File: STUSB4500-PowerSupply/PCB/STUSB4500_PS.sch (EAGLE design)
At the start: 90 parts, among them J2 FEMALE 2x3, J3 FEMALE 2x3, J4 FEMALE 2x3

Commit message: UART and 3V3
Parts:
- added F1: 6V/0.5A, DD_SparkFun-Fuses:PPTC_HALF-AMP
- added J9: (no value), DD_SparkFun-Connectors:CONN_03LOCK_NO_SILK
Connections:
- new net UART_RX: J9.2, U$8.PA1/ADC_IN1/COMP1_INP/USART4_RX
- new net UART_TX: J9.1, U$8.PA2/ADC_IN2/WKUP4USART2_TX
- net +3V3: now also F1.2
- net GND: now also J9.3
- net VIN_2: now also F1.1
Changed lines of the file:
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@@
 <setting verticaltext="up"/>
 </settings>
-<grid distance="0.1" unitdist="inch" unit="inch" style="lines" multiple="1" display="no" altdistance="0.01" altunitdist="inch" altunit="inch"/>
+<grid distance="0.05" unitdist="inch" unit="inch" style="lines" multiple="1" display="no" altdistance="0.01" altunitdist="inch" altunit="inch"/>
 <layers>
 <layer number="1" name="Top" color="4" fill="1" visible="no" active="no"/>
@@
 <part name="+3V15" library="supply1" library_urn="urn:adsk.eagle:library:371" deviceset="+3V3" device=""/>
 <part name="GND5" library="supply1" library_urn="urn:adsk.eagle:library:371" deviceset="GND" device=""/>
+<part name="J9" library="DD_SparkFun-Connectors" deviceset="CONN_03" device="LOCK_NO_SILK"/>
+<part name="GND6" library="supply1" library_urn="urn:adsk.eagle:library:371" deviceset="GND" device=""/>
+<part name="F1" library="DD_SparkFun-Fuses" deviceset="PPTC" device="_HALF-AMP" value="6V/0.5A"/>
+<part name="+3V16" library="supply1" library_urn="urn:adsk.eagle:library:371" deviceset="+3V3" device=""/>
 </parts>
 <sheets>
@@
 <attribute name="VALUE" x="231.14" y="48.26" size="1.778" layer="96"/>
 </instance>
+<instance part="J9" gate="J$1" x="219.71" y="147.32" smashed="yes" rot="R180">
+<attribute name="VALUE" x="222.25" y="154.686" size="1.778" layer="96" font="vector" rot="R180"/>
+<attribute name="NAME" x="222.25" y="141.732" size="1.778" layer="95" font="vector" rot="R180"/>
+</instance>
+<instance part="GND6" gate="1" x="209.55" y="139.7" smashed="yes">
+<attribute name="VALUE" x="207.01" y="137.16" size="1.778" layer="96"/>
+</instance>
+<instance part="F1" gate="G$1" x="53.34" y="152.4" smashed="yes">
+<attribute name="NAME" x="55.245" y="155.575" size="1.778" layer="95" font="vector" align="bottom-center"/>
+<attribute name="VALUE" x="54.61" y="149.606" size="1.778" layer="96" font="vector" align="top-center"/>
+</instance>
+<instance part="+3V16" gate="G$1" x="62.23" y="156.21" smashed="yes">
+<attribute name="VALUE" x="59.69" y="156.21" size="1.778" layer="96"/>
+</instance>
 </instances>
 <busses>
@@
 <wire x1="213.36" y1="104.14" x2="213.36" y2="96.52" width="0.1524" layer="91"/>
 <junction x="213.36" y="96.52"/>
+<junction x="226.06" y="96.52"/>
 </segment>
 </net>
@@
 <wire x1="210.82" y1="99.06" x2="226.06" y2="99.06" width="0.1524" layer="91"/>
 <label x="218.44" y="99.06" size="1.778" layer="95"/>
+<junction x="226.06" y="99.06"/>
 </segment>
 </net>
@@
 <pinref part="GND5" gate="1" pin="GND"/>
 </segment>
+<segment>
+<pinref part="J9" gate="J$1" pin="3"/>
+<wire x1="212.09" y1="144.78" x2="209.55" y2="144.78" width="0.1524" layer="91"/>
+<pinref part="GND6" gate="1" pin="GND"/>
+<wire x1="209.55" y1="144.78" x2="209.55" y2="142.24" width="0.1524" layer="91"/>
+</segment>
 </net>
 <net name="+3V3" class="0">
@@
 <wire x1="68.58" y1="83.82" x2="68.58" y2="86.36" width="0.1524" layer="91"/>
 </segment>
+<segment>
+<pinref part="F1" gate="G$1" pin="2"/>
+<wire x1="60.96" y1="152.4" x2="62.23" y2="152.4" width="0.1524" layer="91"/>
+<pinref part="+3V16" gate="G$1" pin="+3V3"/>
+<wire x1="62.23" y1="152.4" x2="62.23" y2="153.67" width="0.1524" layer="91"/>
+</segment>
 </net>
 <net name="SWDIO" class="0">
@@
 <wire x1="38.1" y1="119.38" x2="45.72" y2="119.38" width="0.1524" layer="91"/>
 <label x="40.64" y="119.38" size="1.778" layer="95"/>
+<junction x="45.72" y="119.38"/>
 </segment>
 </net>
@@
 <wire x1="38.1" y1="116.84" x2="45.72" y2="116.84" width="0.1524" layer="91"/>
 <label x="40.64" y="116.84" size="1.778" layer="95"/>
+<junction x="45.72" y="116.84"/>
 </segment>
 </net>
@@
 <wire x1="38.1" y1="114.3" x2="45.72" y2="114.3" width="0.1524" layer="91"/>
 <label x="40.64" y="114.3" size="1.778" layer="95"/>
+<junction x="45.72" y="114.3"/>
 </segment>
 </net>
@@
 <pinref part="R31" gate="G$1" pin="1"/>
 <pinref part="D2" gate="G$1" pin="A"/>
+<junction x="236.22" y="106.68"/>
 </segment>
 </net>
@@
 <wire x1="259.08" y1="106.68" x2="269.24" y2="106.68" width="0.1524" layer="91"/>
 <label x="261.62" y="106.68" size="1.778" layer="95"/>
+<junction x="269.24" y="106.68"/>
 </segment>
 <segment>
@@
 <wire x1="177.8" y1="116.84" x2="190.5" y2="116.84" width="0.1524" layer="91"/>
 <label x="182.88" y="116.84" size="1.778" layer="95"/>
+<junction x="190.5" y="116.84"/>
 </segment>
 </net>
@@
 <junction x="182.88" y="66.04"/>
 <label x="190.5" y="66.04" size="1.778" layer="95"/>
+<junction x="190.5" y="66.04"/>
 </segment>
 </net>
@@
 <junction x="187.96" y="63.5"/>
 <label x="190.5" y="63.5" size="1.778" layer="95"/>
+<junction x="190.5" y="63.5"/>
 </segment>
 </net>
@@
 <wire x1="177.8" y1="119.38" x2="190.5" y2="119.38" width="0.1524" layer="91"/>
 <label x="182.88" y="119.38" size="1.778" layer="95"/>
+<junction x="190.5" y="119.38"/>
 </segment>
 <segment>
@@
 </segment>
 </net>
+<net name="UART_RX" class="0">
+<segment>
+<pinref part="J9" gate="J$1" pin="2"/>
+<wire x1="212.09" y1="147.32" x2="201.93" y2="147.32" width="0.1524" layer="91"/>
+<label x="201.93" y="147.32" size="1.778" layer="95"/>
+<junction x="201.93" y="147.32"/>
+</segment>
+<segment>
+<pinref part="U$8" gate="G$1" pin="PA1/ADC_IN1/COMP1_INP/USART4_RX"/>
+<wire x1="177.8" y1="124.46" x2="190.5" y2="124.46" width="0.1524" layer="91"/>
+<label x="182.88" y="124.46" size="1.778" layer="95"/>
+<junction x="190.5" y="124.46"/>
+</segment>
+</net>
+<net name="UART_TX" class="0">
+<segment>
+<pinref part="J9" gate="J$1" pin="1"/>
+<wire x1="212.09" y1="149.86" x2="201.93" y2="149.86" width="0.1524" layer="91"/>
+<label x="201.93" y="149.86" size="1.778" layer="95"/>
+<junction x="201.93" y="149.86"/>
+</segment>
+<segment>
+<pinref part="U$8" gate="G$1" pin="PA2/ADC_IN2/WKUP4USART2_TX"/>
+<wire x1="177.8" y1="121.92" x2="190.5" y2="121.92" width="0.1524" layer="91"/>
+<label x="182.88" y="121.92" size="1.778" layer="95"/>
+<junction x="190.5" y="121.92"/>
+</segment>
+</net>
+<net name="VIN_2" class="0">
+<segment>
+<pinref part="F1" gate="G$1" pin="1"/>
+<wire x1="48.26" y1="152.4" x2="40.64" y2="152.4" width="0.1524" layer="91"/>
+<label x="40.64" y="153.67" size="1.778" layer="95"/>
+<junction x="40.64" y="152.4"/>
+</segment>
+</net>

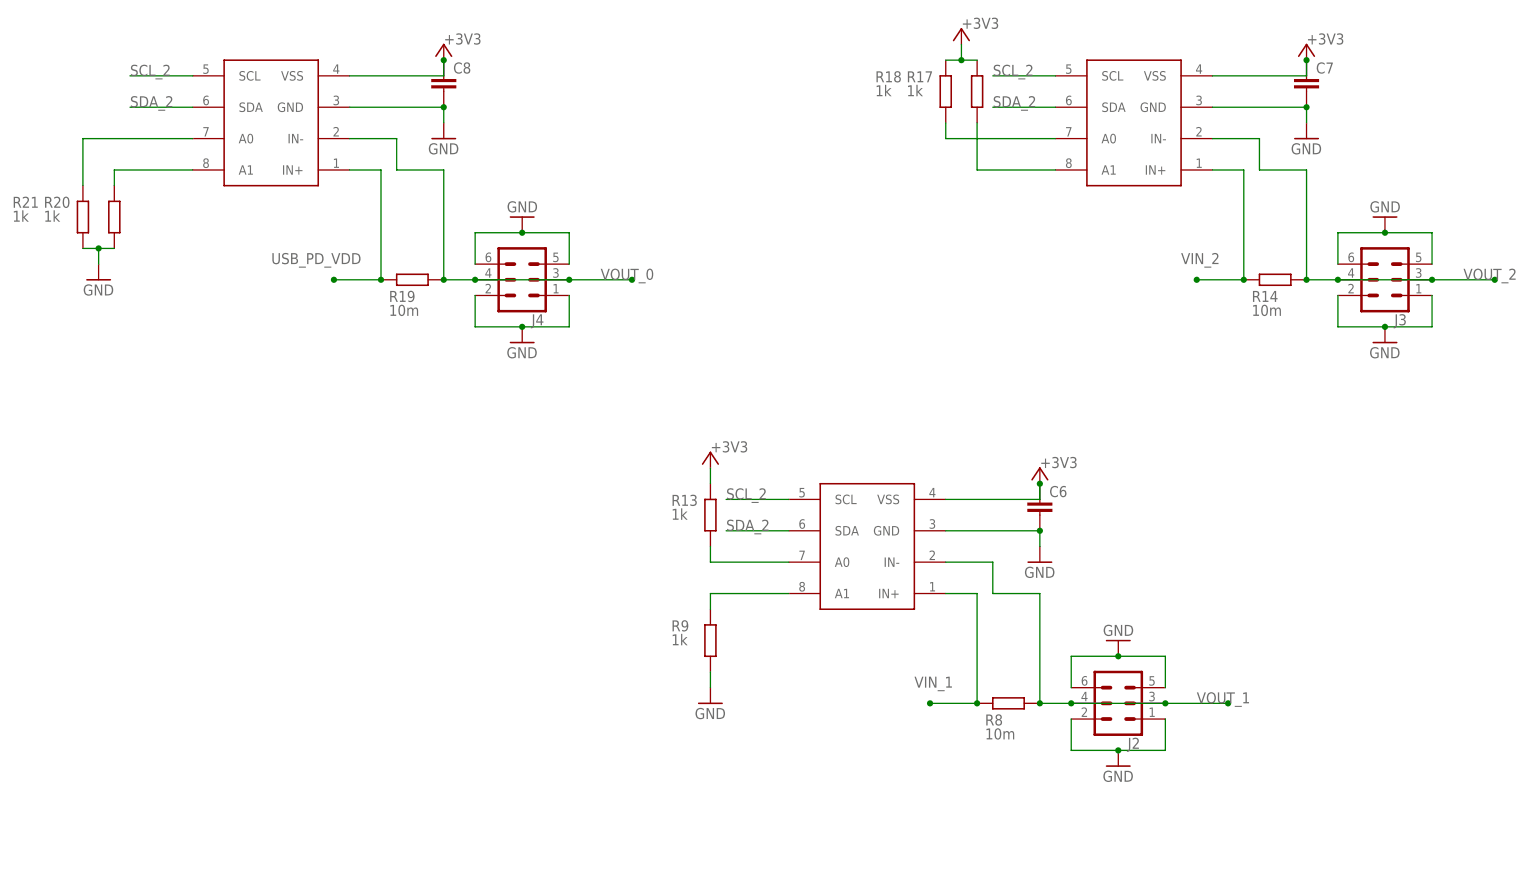
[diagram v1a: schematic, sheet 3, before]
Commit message: Added output caps and diodes
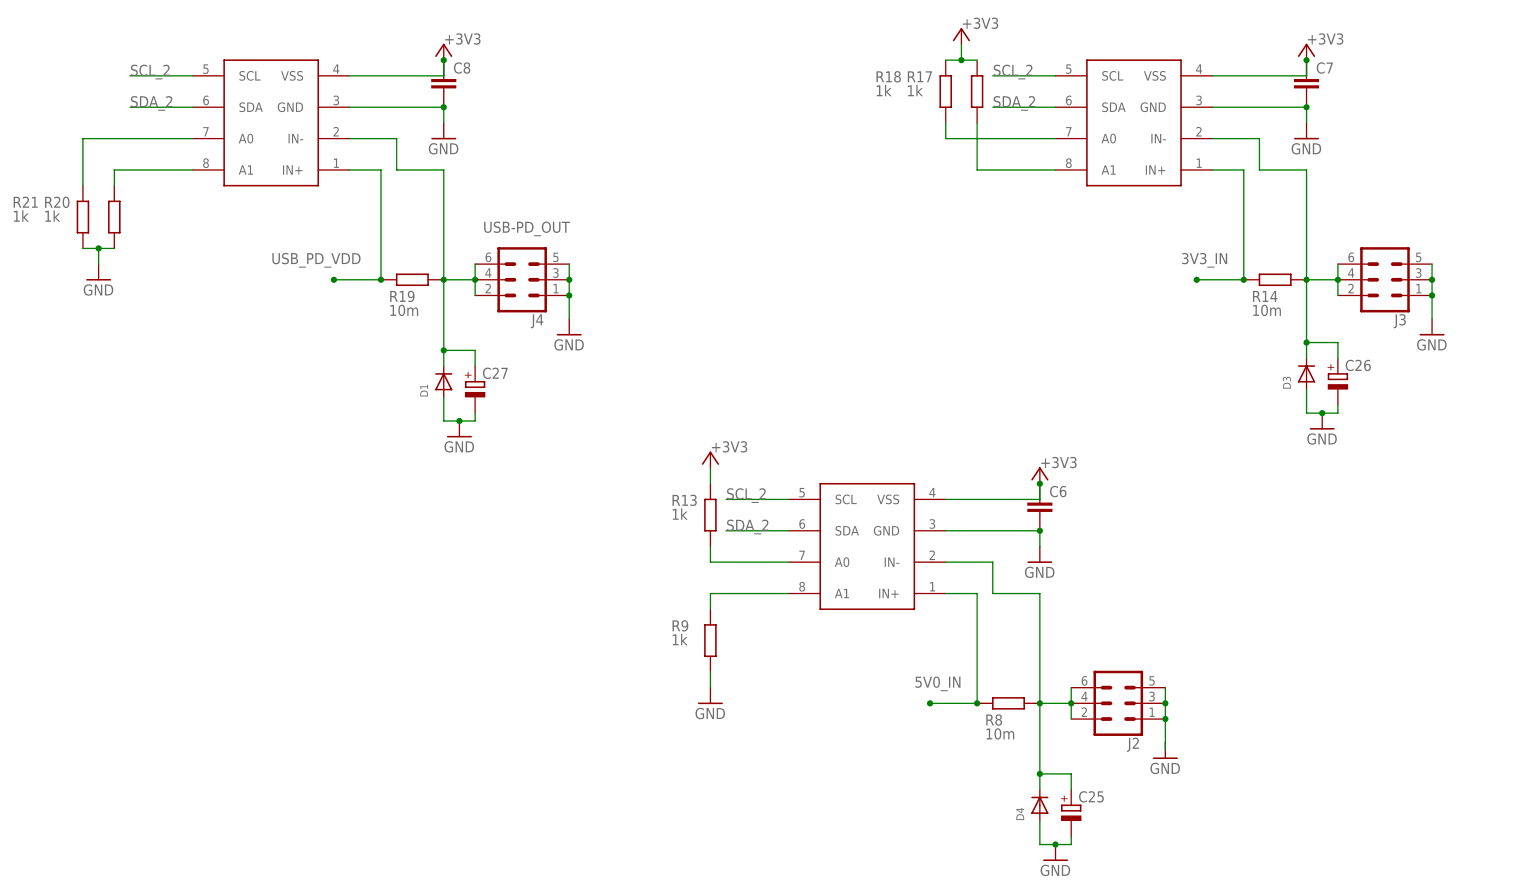
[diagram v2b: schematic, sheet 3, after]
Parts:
- added C25, C26, C27: (no value), DD_rcl:CPOL-EUB/3528-21R
- added D1, D3, D4: (no value), DD_adafruit:DIODE_SOD-123FL
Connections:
- net VIN_1 renamed 5V0_IN
- removed net VOUT_0: J4.3, J4.4, R19.1, U$10.IN-
- removed net VOUT_1: J2.3, J2.4, R8.1, U$7.IN-
- removed net VOUT_2: J3.3, J3.4, R14.1, U$9.IN-
- new net 3V3_IN: C13.2, L2.2, R14.2, R24.2, U$9.IN+
- new net 3V3_OUT: C26.+, D3.C, J3.2, J3.4, J3.6, R14.1, U$9.IN-
- new net 5V0_OUT: C25.+, D4.C, J2.2, J2.4, J2.6, R8.1, U$7.IN-
- new net USB-PD_OUT: C27.+, D1.C, J4.2, J4.4, J4.6, R19.1, U$10.IN-
- net GND: now also C25.-, C26.-, C27.-, D1.A, D3.A, D4.A, J2.3, J3.3, J4.3; no longer J2.2, J2.6, J3.2, J3.6, J4.2, J4.6
- net VIN_2: no longer C13.2, L2.2, R14.2, R24.2, U$9.IN+

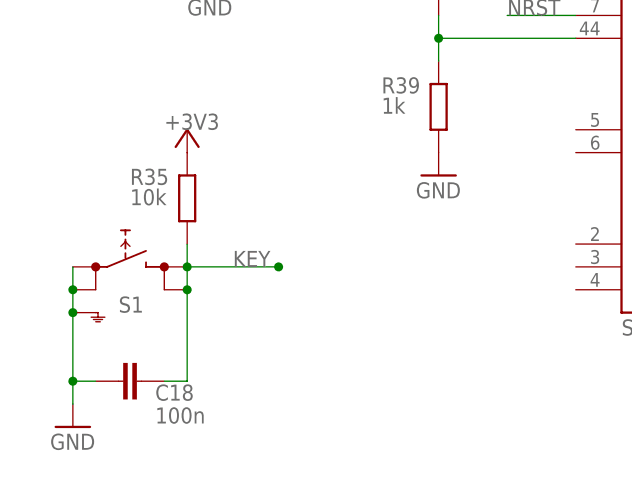
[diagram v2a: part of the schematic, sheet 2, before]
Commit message: Cleanups replaced button with adafruit one
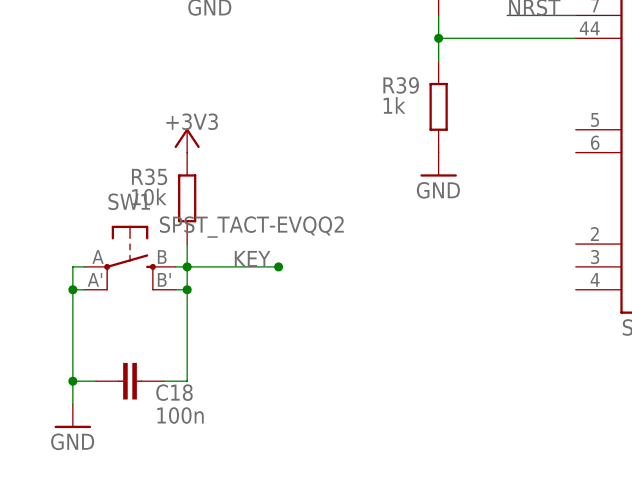
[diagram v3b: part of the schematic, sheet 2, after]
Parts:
- removed S1: SKHMPSE010, switch:SKHMPSE010
- added SW1: SPST_TACT-EVQQ2, DD_adafruit:SPST_TACT-EVQQ2
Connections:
- net GND: now also SW1.P, SW1.P1; no longer S1.1.1, S1.1.2, S1.SH
- net KEY: now also SW1.S, SW1.S1; no longer S1.2.1, S1.2.2

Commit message: Updated stusb part
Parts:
- removed C1, C2: 1u, DD_rcl:C-EUC0402
- removed C3: 100n, DD_rcl:C-EUC0402
- removed C4: 4.7u, DD_rcl:C-EUC1206
- removed C5: 1u, DD_rcl:C-EUC1206
- removed ESDA25W: ESDA25WSOT323, DD_STUSB4500:ESDA25WSOT323
- removed J5: (no value), DD_SparkFun-Connectors:CONN_031.27
- removed J6: (no value), DD_SparkFun-Connectors:CONN_021.27
- removed J7: (no value), DD_SparkFun-Connectors:CONN_02LOCK
- removed J8: (no value), DD_SparkFun-Connectors:CONN_051.27MM
- removed LED1: GM1WA55311A, led:GM1WA55311A
- removed R1, R10, R7: 1k, DD_rcl:R-EU_R0402
- removed R2, R3, R36, R5: 22k, DD_rcl:R-EU_R0402
- removed R4: 100k, DD_rcl:R-EU_R0402
- removed R6: 100, DD_rcl:R-EU_R0402
- removed U$1: STUSB4500QFN24_4X4, DD_STUSB4500:STUSB4500QFN24_4X4
- removed U$2: USB-C, DD_usb_c:USB-C
- removed U$4, U$5: ESDA25P35, DD_STUSB4500:ESDA25P35
- removed U$6: STL6P3LLH6, DD_STUSB4500:STL6P3LLH6
- added C28, C29: 1u, DD_rcl:C-EUC0402
- added C30: 100n, DD_rcl:C-EUC0402
- added C31: 4.7u, DD_rcl:C-EUC1206
- added C32: 1u, DD_rcl:C-EUC1206
- added ESDA25W1: ESDA25WSOT323, DD_STUSB4500:ESDA25WSOT323
- added J10: (no value), DD_SparkFun-Connectors:CONN_02LOCK
- added J11: (no value), DD_SparkFun-Connectors:CONN_051.27MM
- added J12: (no value), DD_SparkFun-Connectors:CONN_021.27
- added J13: (no value), DD_SparkFun-Connectors:CONN_031.27
- added LED2: GM1WA55311A, led:GM1WA55311A
- added R32, R44, R45: 1k, DD_rcl:R-EU_R0402
- added R41: 100k, DD_rcl:R-EU_R0402
- added R42, R46, R47, R48: 22k, DD_rcl:R-EU_R0402
- added R43: 100, DD_rcl:R-EU_R0402
- added U$13: USB-C, DD_usb_c:USB-C
- added U$14, U$15: ESDA25P35, DD_STUSB4500:ESDA25P35
- added U$16: STL6P3LLH6, DD_STUSB4500:STL6P3LLH6
- added U$3: STUSB4500QFN24_4X4, DD_STUSB4500:STUSB4500QFN24_4X4
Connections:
- removed net N$10: ESDA25W.CC1, U$1.CC1, U$1.CC1DB, U$2.A5_CC1
- removed net N$11: ESDA25W.CC2, U$1.CC2, U$1.CC2DB, U$2.B5_CC2
- removed net N$12: R5.1, U$1.VBUS_EN_SNK
- removed net N$14: R10.2, U$1.DISCH
- removed net N$16: C1.1, U$1.VREG_2V7
- removed net N$17: C2.1, U$1.VREG_1V2
- removed net N$2: LED1.CGREEN, R2.2
- removed net N$20: LED1.CBLUE, R36.2
- removed net N$3: R4.1, R5.2, R6.2, U$6.G
- removed net N$5: R7.2, U$1.VBUS_VS_DISCH
- removed net N$6: LED1.CRED, R3.2
- removed net N$7: C3.1, R6.1
- new net N$21: R41.1, R42.2, R43.2, U$16.G
- new net N$31: R44.2, U$3.VBUS_VS_DISCH
- new net N$32: ESDA25W1.CC1, U$13.A5_CC1, U$3.CC1, U$3.CC1DB
- new net N$33: ESDA25W1.CC2, U$13.B5_CC2, U$3.CC2, U$3.CC2DB
- new net N$34: R42.1, U$3.VBUS_EN_SNK
- new net N$42: C30.1, R43.1
- new net N$43: R45.2, U$3.DISCH
- new net N$44: C28.1, U$3.VREG_2V7
- new net N$45: C29.1, U$3.VREG_1V2
- new net N$46: LED2.CGREEN, R46.2
- new net N$47: LED2.CRED, R47.2
- new net N$48: LED2.CBLUE, R48.2
- net GND: now also C28.2, C29.2, C31.2, C32.2, ESDA25W1.GND, J10.2, J13.3, R32.1, R46.1, U$13.A12_GND, U$13.A1_GND, U$13.B12_GND, U$13.B1_GND, U$13.SHIELD, U$14.GND, U$15.GND, U$3.ADDR0, U$3.ADDR1, U$3.GND, U$3.PAD, U$3.VCONN, U$3.VSYS; no longer C1.2, C2.2, C4.2, C5.2, ESDA25W.GND, J5.3, J7.2, R1.1, R2.1, U$1.ADDR0, U$1.ADDR1, U$1.GND, U$1.PAD, U$1.VCONN, U$1.VSYS, U$2.A12_GND, U$2.A1_GND, U$2.B12_GND, U$2.B1_GND, U$2.SHIELD, U$4.GND, U$5.GND
- net SCL: now also J11.2, U$3.SCL; no longer J8.2, U$1.SCL
- net SDA: now also J11.3, U$3.SDA; no longer J8.3, U$1.SDA
- net STUSB_AB: now also J13.2, U$3.A-B_SIDE; no longer J5.2, U$1.A-B_SIDE
- net STUSB_ALERT: now also J11.5, U$3.ALERT; no longer J8.5, U$1.ALERT
- net STUSB_ATTACH: now also J11.4, U$3.ATTACH; no longer J8.4, U$1.ATTACH
- net STUSB_GPIO: now also J13.1, U$3.GPIO; no longer J5.1, U$1.GPIO
- net STUSB_PDO2: now also R47.1, U$3.PDO2; no longer R3.1, U$1.PDO2
- net STUSB_PDO3: now also R48.1, U$3.PDO3; no longer R36.1, U$1.PDO3
- net STUSB_RST: now also J11.1, R32.2, U$3.RESET; no longer J8.1, R1.2, U$1.RESET
- net USB_D+: now also J12.1, U$13.A6_D+, U$13.B6_D+; no longer J6.1, U$2.A6_D+, U$2.B6_D+
- net USB_D-: now also J12.2, U$13.A7_D-, U$13.B7_D-; no longer J6.2, U$2.A7_D-, U$2.B7_D-
- net USB_PD_VDD: now also C30.2, C32.1, J10.1, LED2.A, R45.1, U$15.VBUS, U$16.D; no longer C3.2, C5.1, J7.1, LED1.A, R10.1, U$5.VBUS, U$6.D
- net VDD: now also C31.1, R41.2, R44.1, U$13.A4_VBUS, U$13.A9_VBUS, U$13.B4_VBUS, U$13.B_VBUS, U$14.VBUS, U$16.S, U$3.VDD; no longer C4.1, R4.2, R7.1, U$1.VDD, U$2.A4_VBUS, U$2.A9_VBUS, U$2.B4_VBUS, U$2.B_VBUS, U$4.VBUS, U$6.S

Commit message: Cleanups in BOM, fixed OLED layout
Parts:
- C10, C13: value (none) -> 22uF 6.3V
- C11, C14: value (none) -> 10uF 25V
- C12, C6, C7, C8, C9: value (none) -> 100nF 25V; device DD_rcl:C-EUC0603 -> DD_rcl:C-EUC0402
- C15, C16, C17, C18, C19: value 100n -> 100nF 25V; device DD_rcl:C-EUC0603 -> DD_rcl:C-EUC0402
- C20, C21: value (none) -> 10uF 6.3V
- C22, C23, C24: value (none) -> 1uF 25V
- C25, C26: value (none) -> 22uF 6.3V; device DD_rcl:CPOL-EUB/3528-21R -> DD_rcl:C-EUC1206
- C27: value (none) -> 10uF 25V; device DD_rcl:CPOL-EUB/3528-21R -> DD_rcl:C-EUC1206
- C28, C29: value 1u -> 1uF 6.3V
- C30: value 100n -> 100nF 25V
- C31: value 4.7u -> 10uF 25V
- C32: value 1u -> 10uF 25V
- L1: value (none) -> 5.6uH
- L2: value (none) -> 4.7uH
- R11, R23: value (none) -> 30
- R12: value (none) -> 52.3k; device DD_rcl:R-EU_R0805 -> DD_rcl:R-EU_R0603
- R14, R19, R8: value 10m -> 0.1R
- R15, R25: value (none) -> 10k; device DD_rcl:R-EU_R0805 -> DD_rcl:R-EU_R0603
- R24: value (none) -> 31.6k; device DD_rcl:R-EU_R0805 -> DD_rcl:R-EU_R0603
- R31: value 10K -> 10k; device DD_rcl:R-EU_R0603 -> DD_rcl:R-EU_R0402
- R35: device DD_rcl:R-EU_R0603 -> DD_rcl:R-EU_R0402
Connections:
- net 3V3_OUT: now also C26.1; no longer C26.+
- net 5V0_OUT: now also C25.1; no longer C25.+
- net GND: now also C25.2, C26.2, C27.2; no longer C25.-, C26.-, C27.-
- net USB-PD_OUT: now also C27.1; no longer C27.+
